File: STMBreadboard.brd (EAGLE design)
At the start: 100 x 80 mm, 27 parts, among them IC1 REG1117, Y1 8MHz

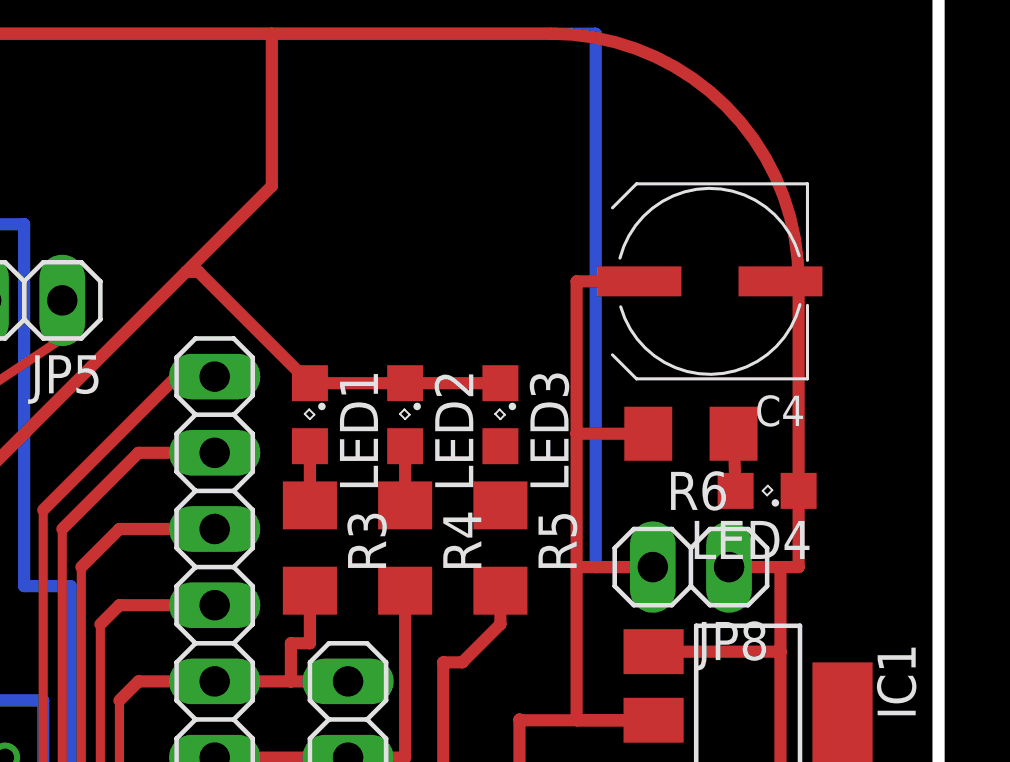
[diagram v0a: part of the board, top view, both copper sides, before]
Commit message: LED 0603
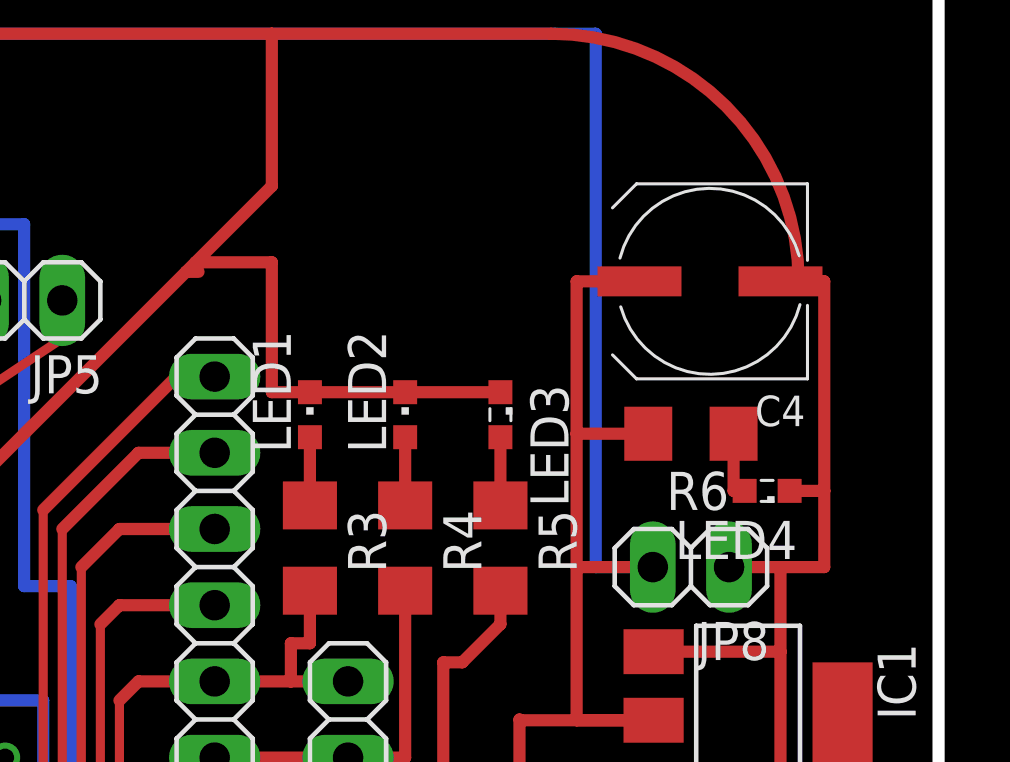
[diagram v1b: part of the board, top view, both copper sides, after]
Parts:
- LED1, LED2: device led:SML0805 -> led:CHIPLED_0603
- LED3, LED4: device led:SML0805 -> led:SML0603
- turned LED1 to 0 degrees
- turned LED2 to 0 degrees
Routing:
- net GND: track 224.7 -> 230.4 mm
- net N$6: track 0.00 -> 2.27 mm
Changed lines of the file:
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@@
 <element name="JP7" library="jumper" package="JP1" value="" x="35.56" y="29.21" rot="R270"/>
 <element name="JP8" library="pinhead" package="1X02" value="3VOUT" x="71.12" y="43.815" rot="R180"/>
-<element name="LED1" library="led" package="SML0805" value="" x="58.42" y="48.895" rot="R270"/>
-<element name="LED2" library="led" package="SML0805" value="" x="61.595" y="48.895" rot="R270"/>
-<element name="LED3" library="led" package="SML0805" value="" x="64.77" y="48.895" rot="R270"/>
-<element name="LED4" library="led" package="SML0805" value="" x="73.66" y="46.355" rot="R180"/>
+<element name="LED1" library="led" package="CHIPLED_0603" value="" x="58.42" y="48.895"/>
+<element name="LED2" library="led" package="CHIPLED_0603" value="" x="61.595" y="48.895"/>
+<element name="LED3" library="led" package="SML0603" value="" x="64.77" y="48.895" rot="R270"/>
+<element name="LED4" library="led" package="SML0603" value="" x="73.66" y="46.355" rot="R180"/>
 <element name="R1" library="rcl" package="R1206" value="10k" x="52.705" y="26.035"/>
 <element name="R2" library="rcl" package="R1206" value="10k" x="31.115" y="27.94" rot="R90"/>
@@
 <wire x1="37.465" y1="59.055" x2="37.465" y2="61.595" width="0.4064" layer="1"/>
 <wire x1="72.39" y1="43.815" x2="74.105" y2="43.815" width="0.4064" layer="1"/>
-<wire x1="74.71" y1="46.355" x2="74.71" y2="53.34" width="0.4064" layer="1"/>
 <wire x1="74.71" y1="53.34" x2="74.105" y2="53.34" width="0.4064" layer="1"/>
-<wire x1="74.71" y1="46.355" x2="74.71" y2="43.815" width="0.4064" layer="1"/>
-<wire x1="74.71" y1="43.815" x2="74.105" y2="43.815" width="0.4064" layer="1"/>
 <wire x1="37.465" y1="61.595" x2="57.15" y2="61.595" width="0.4064" layer="1"/>
 <wire x1="57.15" y1="61.595" x2="66.455" y2="61.595" width="0.4064" layer="1"/>
@@
 <wire x1="45.72" y1="46.355" x2="46.99" y2="46.355" width="0.4064" layer="1"/>
 <wire x1="46.99" y1="46.355" x2="54.2925" y2="53.6575" width="0.4064" layer="1"/>
-<wire x1="54.2925" y1="53.6575" x2="57.15" y2="56.515" width="0.4064" layer="1"/>
+<wire x1="54.2925" y1="53.6575" x2="54.61" y2="53.975" width="0.4064" layer="1"/>
+<wire x1="54.61" y1="53.975" x2="57.15" y2="56.515" width="0.4064" layer="1"/>
 <wire x1="57.15" y1="56.515" x2="57.15" y2="61.595" width="0.4064" layer="1"/>
 <wire x1="38.175" y1="34.445" x2="35.715" y2="34.445" width="0.3048" layer="1"/>
@@
 <wire x1="31.115" y1="26.518" x2="31.267" y2="26.518" width="0.4064" layer="1"/>
 <wire x1="31.267" y1="26.518" x2="33.02" y2="24.765" width="0.4064" layer="1"/>
-<wire x1="58.42" y1="49.945" x2="61.595" y2="49.945" width="0.4064" layer="1"/>
-<wire x1="64.77" y1="49.945" x2="61.595" y2="49.945" width="0.4064" layer="1"/>
-<wire x1="58.42" y1="49.945" x2="54.7075" y2="53.6575" width="0.4064" layer="1"/>
 <wire x1="54.7075" y1="53.6575" x2="54.2925" y2="53.6575" width="0.4064" layer="1"/>
+<wire x1="64.77" y1="49.645" x2="61.595" y2="49.645" width="0.4064" layer="1"/>
+<wire x1="61.595" y1="49.645" x2="58.42" y2="49.645" width="0.4064" layer="1"/>
+<wire x1="58.42" y1="49.645" x2="57.15" y2="49.645" width="0.4064" layer="1"/>
+<wire x1="57.15" y1="49.645" x2="57.15" y2="53.975" width="0.4064" layer="1"/>
+<wire x1="57.15" y1="53.975" x2="54.61" y2="53.975" width="0.4064" layer="1"/>
+<wire x1="75.565" y1="46.355" x2="75.565" y2="43.815" width="0.4064" layer="1"/>
+<wire x1="75.565" y1="43.815" x2="74.105" y2="43.815" width="0.4064" layer="1"/>
+<wire x1="74.41" y1="46.355" x2="75.565" y2="46.355" width="0.4064" layer="1"/>
+<wire x1="75.565" y1="46.355" x2="75.565" y2="53.34" width="0.4064" layer="1"/>
+<wire x1="75.565" y1="53.34" x2="74.71" y2="53.34" width="0.4064" layer="1"/>
 </signal>
 <signal name="N$3">
@@
 <contactref element="LED1" pad="A"/>
 <contactref element="R3" pad="1"/>
-<wire x1="58.42" y1="45.872" x2="58.42" y2="47.845" width="0.4064" layer="1"/>
+<wire x1="58.42" y1="48.145" x2="58.42" y2="45.872" width="0.4064" layer="1"/>
 </signal>
 <signal name="N$5">
 <contactref element="R4" pad="1"/>
 <contactref element="LED2" pad="A"/>
-<wire x1="61.595" y1="45.872" x2="61.595" y2="47.845" width="0.4064" layer="1"/>
+<wire x1="61.595" y1="48.145" x2="61.595" y2="45.872" width="0.4064" layer="1"/>
 </signal>
 <signal name="N$6">
 <contactref element="R5" pad="1"/>
 <contactref element="LED3" pad="A"/>
-<wire x1="64.77" y1="45.872" x2="64.77" y2="47.845" width="0" layer="19" extent="1-1"/>
+<wire x1="64.77" y1="48.145" x2="64.77" y2="45.872" width="0.4064" layer="1"/>
 </signal>
 <signal name="N$7">
 <contactref element="R6" pad="1"/>
 <contactref element="LED4" pad="A"/>
-<wire x1="72.542" y1="48.26" x2="72.61" y2="46.355" width="0.4064" layer="1"/>
+<wire x1="72.91" y1="46.355" x2="72.542" y2="46.355" width="0.4064" layer="1"/>
+<wire x1="72.542" y1="46.355" x2="72.542" y2="48.26" width="0.4064" layer="1"/>
 </signal>
 </signals>

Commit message: LED 0603-002
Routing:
- net GND: vias 0 -> 4
- added copper zone on layer 1, net GND
- added copper zone on layer 16, net GND

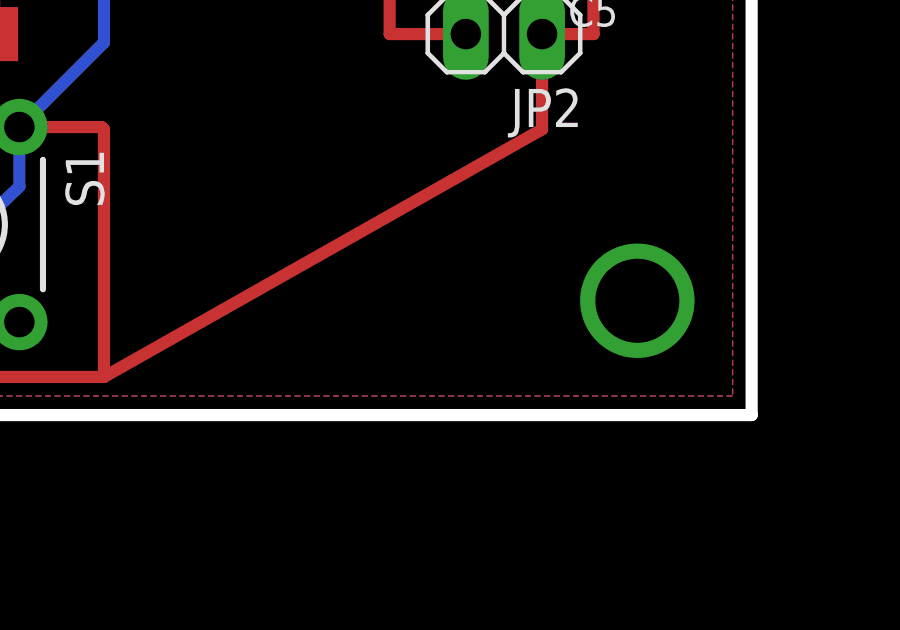
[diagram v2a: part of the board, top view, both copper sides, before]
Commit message: inkscape PCB image for laser iron technology added
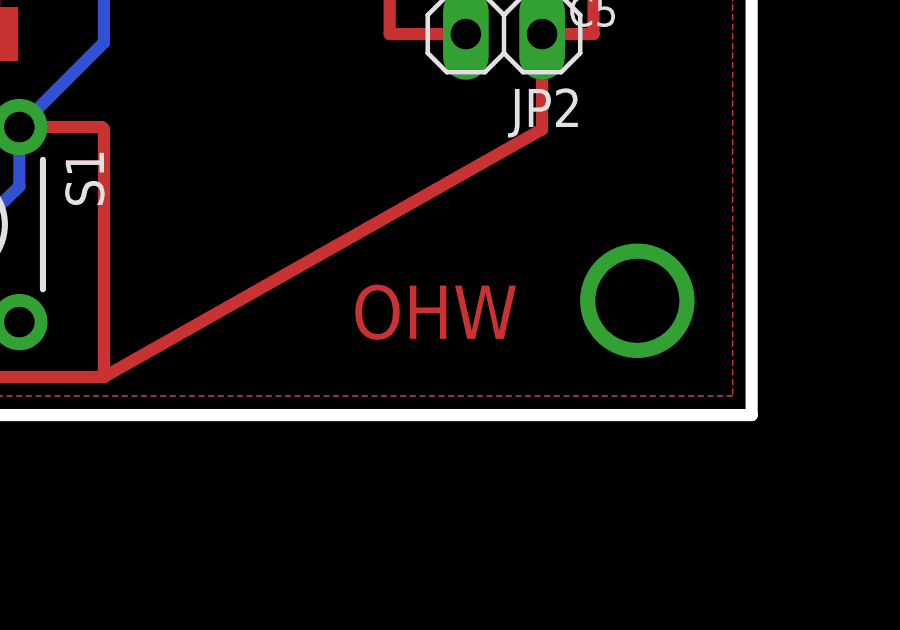
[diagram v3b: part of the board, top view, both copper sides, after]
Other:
- board text added: "OHW"
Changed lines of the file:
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@@
 <dimension x1="23.495" y1="13.335" x2="79.375" y2="13.335" x3="51.435" y3="8.255" textsize="1.778" layer="20"/>
 <dimension x1="79.375" y1="13.335" x2="79.375" y2="64.135" x3="83.82" y3="38.735" textsize="1.778" layer="20"/>
+<text x="66.04" y="15.875" size="1.778" layer="1">OHW</text>
 </plain>
 <attributes>
@@
 <via x="75.565" y="60.325" extent="1-16" drill="2.8" diameter="1.6764" shape="octagon"/>
 <via x="27.305" y="60.325" extent="1-16" drill="2.8" shape="octagon"/>
-<wire x1="37.465" y1="59.055" x2="27.305" y2="60.325" width="0" layer="19" extent="1-1"/>
 </signal>
 <signal name="N$3">
